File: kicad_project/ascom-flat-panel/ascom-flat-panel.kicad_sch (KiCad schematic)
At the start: 12 parts, among them J1 Servo, J3 JST-XH LED, Q1 IRLZ34N, Q2 IRLZ34N, U1 XIAO-SAMD21-DIP

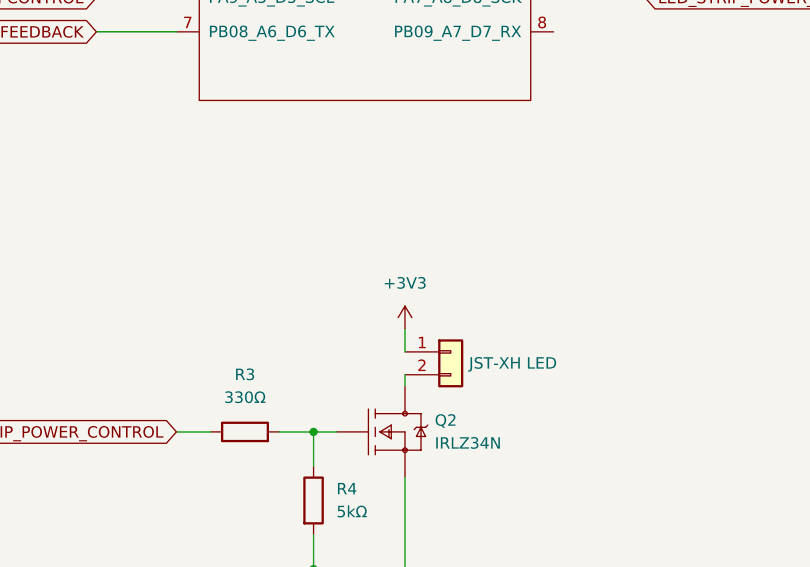
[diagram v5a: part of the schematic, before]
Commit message: [kicad] - schéma : alimentation des LEDs passée de 3V3 à 5V suite aux tests
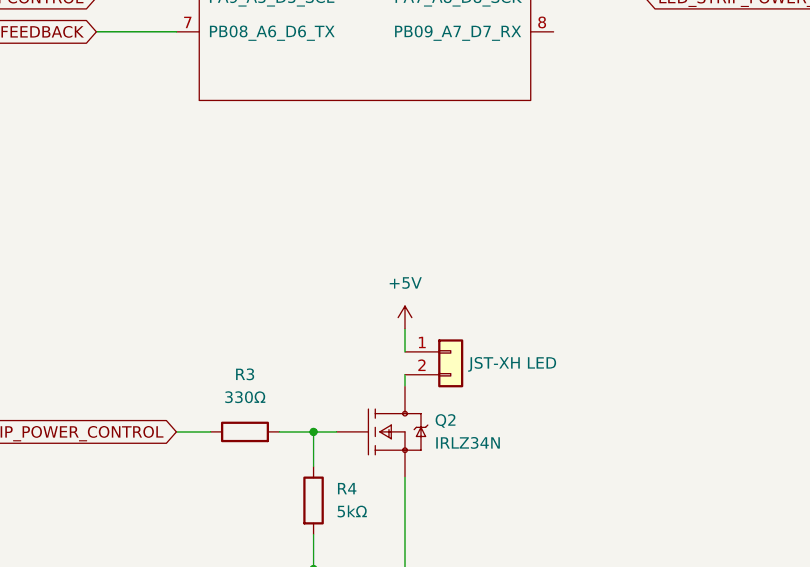
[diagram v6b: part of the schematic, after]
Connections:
- net +3V3: no longer J3.1 (Pin_1)
- net +5V: now also J3.1 (Pin_1)
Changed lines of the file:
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@@
-	)
-	(symbol
-		(lib_id "power:+3V3")
-		(at 88.9 100.33 0)
-		(unit 1)
-		(exclude_from_sim no)
-		(in_bom yes)
-		(on_board yes)
-		(dnp no)
-		(fields_autoplaced yes)
-		(property "Reference" "#PWR08"
-			(at 88.9 104.14 0)
-			(effects
-				(font
-					(size 1.27 1.27)
-				)
-				(hide yes)
-			)
-		)
-		(property "Value" "+3V3"
-			(at 88.9 95.25 0)
-			(effects
-				(font
-					(size 1.27 1.27)
-				)
-			)
-		)
-		(property "Footprint" ""
-			(at 88.9 100.33 0)
-			(effects
-				(font
-					(size 1.27 1.27)
-				)
-				(hide yes)
-			)
-		)
-		(property "Datasheet" ""
-			(at 88.9 100.33 0)
-			(effects
-				(font
-					(size 1.27 1.27)
-				)
-				(hide yes)
-			)
-		)
-		(property "Description" "Power symbol creates a global label with name \"+3V3\""
-			(at 88.9 100.33 0)
-			(effects
-				(font
-					(size 1.27 1.27)
-				)
-				(hide yes)
-			)
-		)
-		(pin "1"
-		)
-		(instances
-			(project ""
-				(path "/c93103f3-9ac9-4319-baa6-df31525a6c92"
-					(reference "#PWR08")
-					(unit 1)
-				)
-			)
-		)
 	)
 	(symbol
@@
 					(unit 1)
 				)
+			)
+		)
+	)
+	(symbol
+		(lib_name "+5V_1")
+		(lib_id "power:+5V")
+		(at 88.9 100.33 0)
+		(unit 1)
+		(exclude_from_sim no)
+		(in_bom yes)
+		(on_board yes)
+		(dnp no)
+		(fields_autoplaced yes)
+		(property "Reference" "#PWR08"
+			(at 88.9 104.14 0)
+			(effects
+				(font
+					(size 1.27 1.27)
+				)
+				(hide yes)
+			)
+		)
+		(property "Value" "+5V"
+			(at 88.9 95.25 0)
+			(effects
+				(font
+					(size 1.27 1.27)
+				)
+			)
+		)
+		(property "Footprint" ""
+			(at 88.9 100.33 0)
+			(effects
+				(font
+					(size 1.27 1.27)
+				)
+				(hide yes)
+			)
+		)
+		(property "Datasheet" ""
+			(at 88.9 100.33 0)
+			(effects
+				(font
+					(size 1.27 1.27)
+				)
+				(hide yes)
+			)
+		)
+		(property "Description" "Power symbol creates a global label with name \"+5V\""
+			(at 88.9 100.33 0)
+			(effects
+				(font
+					(size 1.27 1.27)
+				)
+				(hide yes)
+			)
+		)
+		(pin "1"
+		)
+		(instances
+			(project ""
+				(path "/c93103f3-9ac9-4319-baa6-df31525a6c92"
+					(reference "#PWR08")
+					(unit 1)
+				)

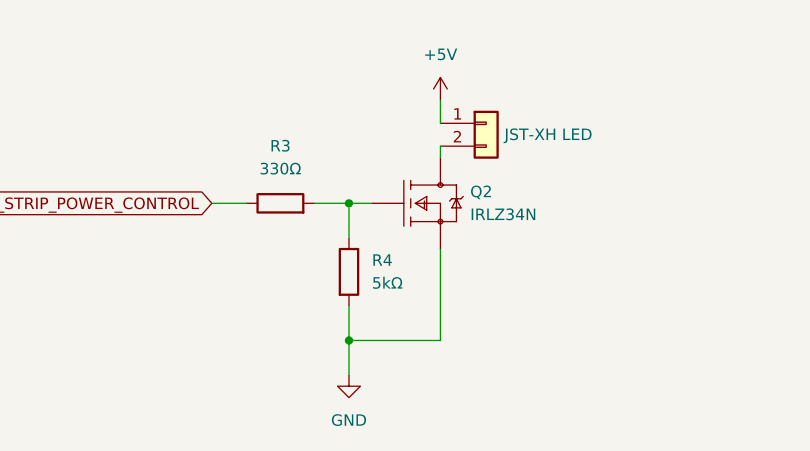
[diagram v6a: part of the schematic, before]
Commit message: [kicad] - mise à jour valeur résistance 5k -> 4k7 suivant tests + ajustement de routage
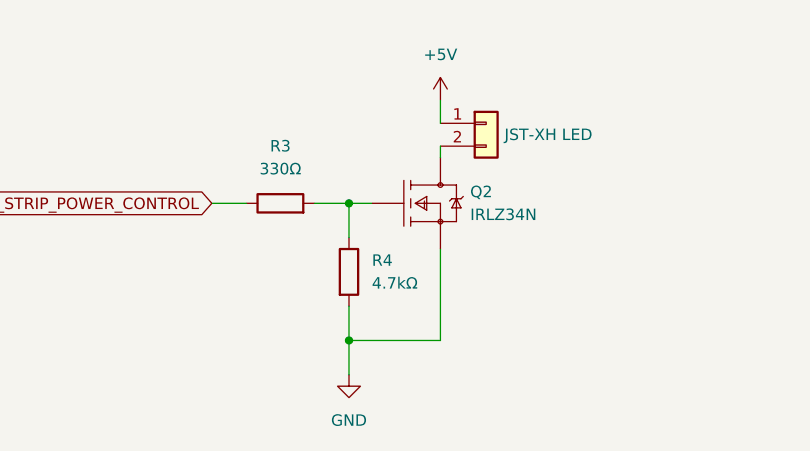
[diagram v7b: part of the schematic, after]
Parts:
- R4: value 5kΩ -> 4.7kΩ
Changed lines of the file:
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@@
 			)
 		)
-		(property "Value" "5kΩ"
+		(property "Value" "4.7kΩ"
 			(at 81.28 120.6499 0)
 			(effects

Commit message: [kicad] - renommage connecteur J3 -> J2
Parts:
- renumbered J3 to J2
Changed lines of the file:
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@@
 		(on_board yes)
 		(dnp no)
-		(property "Reference" "J3"
+		(property "Reference" "J2"
 			(at 97.028 102.8699 0)
 			(effects
@@
 			(project "ascom-flat-panel"
 				(path "/c93103f3-9ac9-4319-baa6-df31525a6c92"
-					(reference "J3")
+					(reference "J2")
 					(unit 1)
 				)
